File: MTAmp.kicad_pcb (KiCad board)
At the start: 2 copper layers, 67.3 x 86.4 mm, 31 parts, among them J1 IN3, J10 AMP1, J11 AMP2, J12 PROG, J2 PWR, J3 IN1, J4 IN4, J5 IN2, J6 OUT1, J7 OUT2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

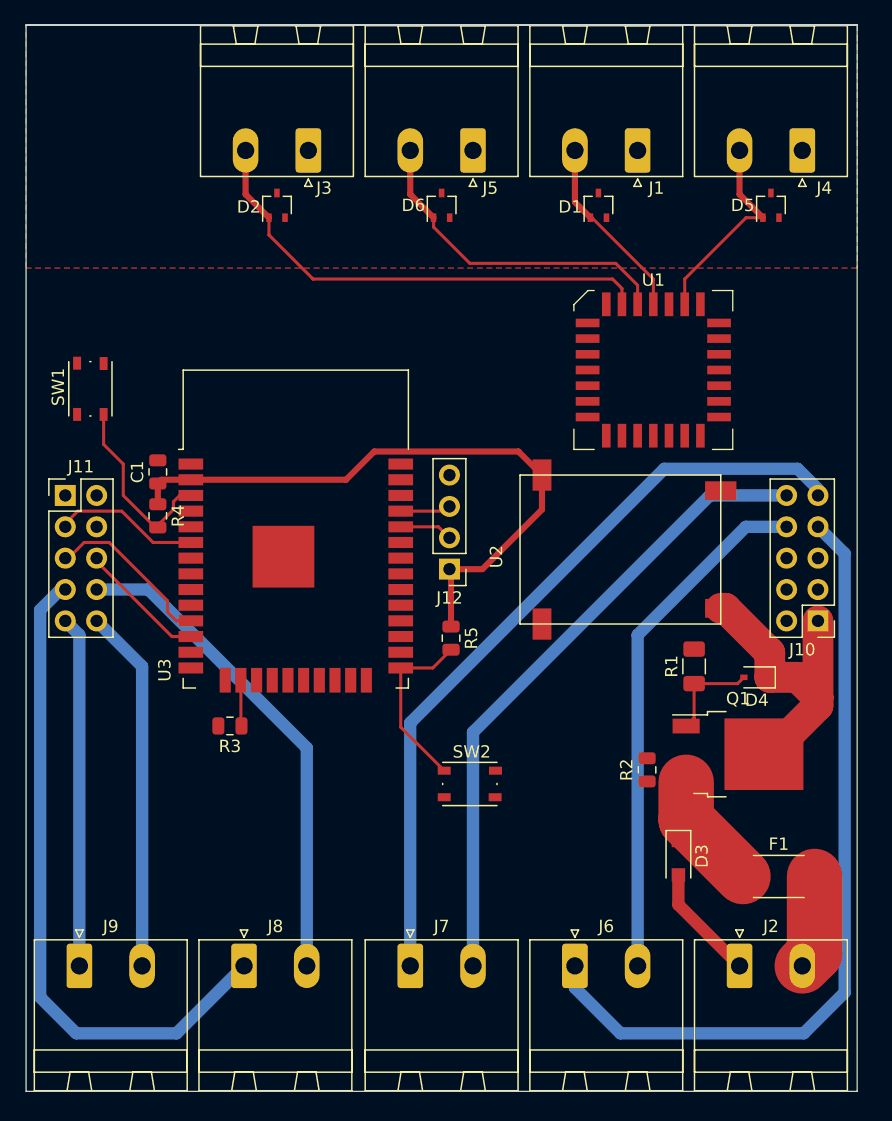
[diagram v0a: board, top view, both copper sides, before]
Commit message: Main PCB traced
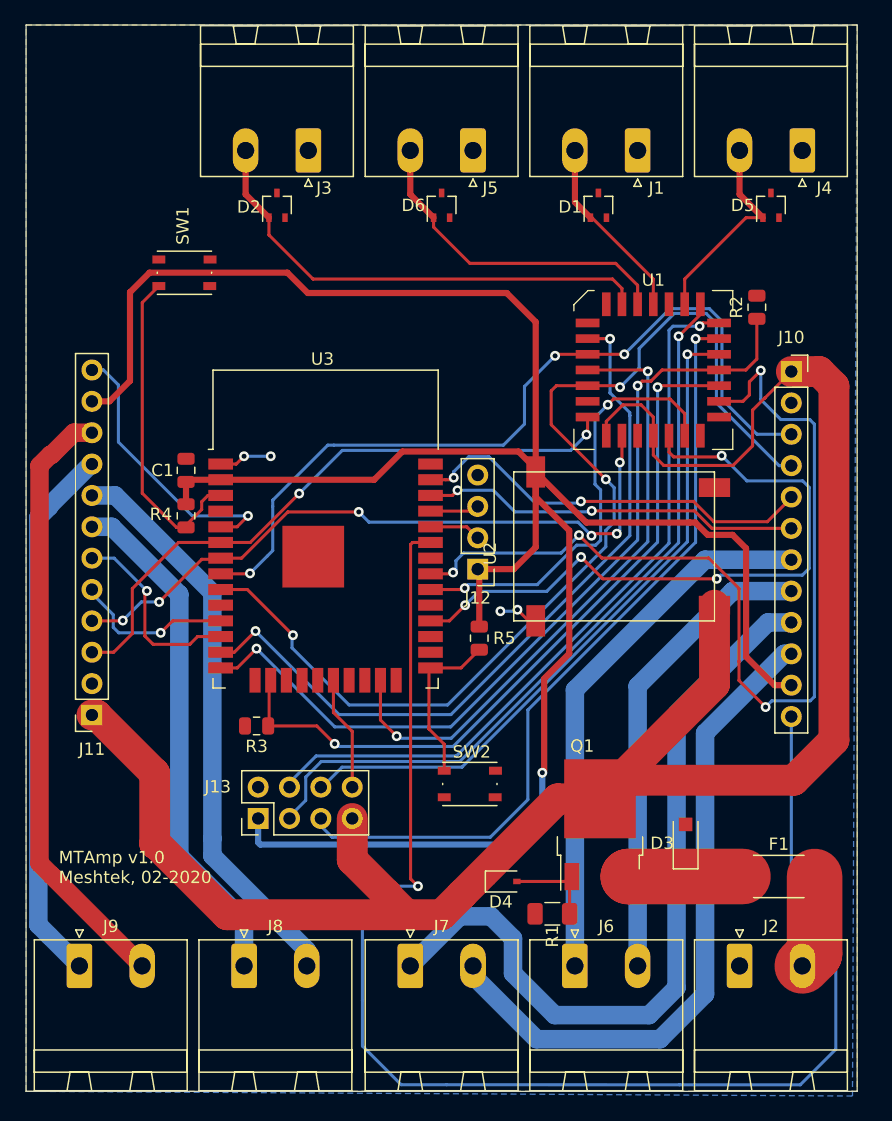
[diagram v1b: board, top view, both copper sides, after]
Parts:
- added J13: BT, Connector_PinHeader_2.54mm:PinHeader_2x04_P2.54mm_Vertical, F.Cu at (131.8, 90.9)
- J10, J11: footprint Connector_PinHeader_2.54mm:PinHeader_2x05_P2.54mm_Vertical -> Connector_PinSocket_2.54mm:PinSocket_1x12_P2.54mm_Vertical
- moved R2 38.5 mm to (172.2, 49.5)
- moved D4 26.3 mm to (151.7, 96.0), turned to 0 degrees
- moved R1 23.1 mm to (155.7, 98.7), turned to 180 degrees
- moved J10 20.3 mm to (175.0, 54.7), turned to 0 degrees
- moved J11 17.9 mm to (118.4, 82.5), turned to 180 degrees
- moved Q1 12.6 mm to (159.5, 91.4), turned to 90 degrees
- moved SW1 12.1 mm to (125.9, 46.7), turned to 0 degrees
- moved U3 2.41 mm to (137.3, 70.5)
- moved C1 2.29 mm to (126.0, 62.7)
- moved J12 2.29 mm to (149.6, 70.7)
- moved R4 2.29 mm to (126.0, 66.4)
- moved R5 2.29 mm to (149.7, 76.3)
- moved R3 2.16 mm to (131.7, 83.4)
- moved D3 1.42 mm to (166.4, 92.8), turned to 90 degrees
- moved U2 0.57 mm to (152.5, 74.9)
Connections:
- C1 pad 2: GNDD -> GNDA
- D3 pad 2: Net-(D3-Pad2) -> GNDA
- J10 pad 2: AGND -> GNDA
- J11 pad 2: AGND -> GNDA
- J12 pad 4: GNDD -> GNDA
- J2 pad 1: Net-(D3-Pad2) -> GNDA
- R1 pad 2: Net-(D3-Pad2) -> GNDA
- R2 pad 1: MT_Resest -> MT_Reset
- R2 pad 2: GNDD -> GNDA
- R3 pad 2: GNDD -> GNDA
- SW1 pad 1: GNDD -> GNDA
- SW2 pad 2: GNDD -> GNDA
- U1 pad 22: MT_Resest -> MT_Reset
- U2 pad 2: Net-(D3-Pad2) -> GNDA
- U3 pad 1: GNDD -> GNDA
- U3 pad 10: SD2 -> Net-(U3-Pad10)
- U3 pad 15: GNDD -> GNDA
- U3 pad 20: Net-(U3-Pad20) -> CONNECTED_BT
- U3 pad 33: Net-(U3-Pad33) -> CONNECTED1
- U3 pad 36: Net-(U3-Pad36) -> SD2
- U3 pad 38: GNDD -> GNDA
- U3 pad 39: GNDD -> GNDA
- U3 pad 5: Net-(U3-Pad5) -> CONNECTED2
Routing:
- net +3V3: track 51.6 -> 196.3 mm, vias 0 -> 1
- net +12V: track 24.9 -> 163.1 mm
- net CONNECTED1: track 0.00 -> 114.9 mm, vias 0 -> 1
- net MT_Out2: track 0.00 -> 88.1 mm, vias 0 -> 3
- net MT_AY2: track 0.00 -> 77.9 mm, vias 0 -> 4
- net MT_Reset: track 0.00 -> 69.6 mm, vias 0 -> 2
- net MT_Out1: track 0.00 -> 67.2 mm, vias 0 -> 3
- net MT_In7: track 0.00 -> 63.9 mm, vias 0 -> 1
- net MT_In5: track 0.00 -> 62.0 mm, vias 0 -> 1
- net MT_Data: track 0.00 -> 61.1 mm, vias 0 -> 2
- net MT_In6: track 0.00 -> 60.7 mm, vias 0 -> 1
- net MT_STB: track 3.72 -> 60.3 mm, vias 0 -> 2
- net MT_In8: track 0.00 -> 55.7 mm, vias 0 -> 1
- net MT_Out4: track 0.00 -> 55.1 mm, vias 0 -> 6
- net MT_AY0: track 0.00 -> 54.4 mm, vias 0 -> 4
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- added copper zone on B.Cu, net GNDA
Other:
- net class 3v3: clearance 0.2 -> 0.1
- net class Default: clearance 0.2 -> 0.1
- net class HighPwr: trace_width 1 -> 1.5
- net class IN12: clearance 0.2 -> 0.1
- net class InAudio: clearance 0.2 -> 0.1
- rule trace_clearance: 0.2 -> 0.1
- board text added: "MTAmp v1.0 Meshtek, 02-2020"

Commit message: Added some text on PCB
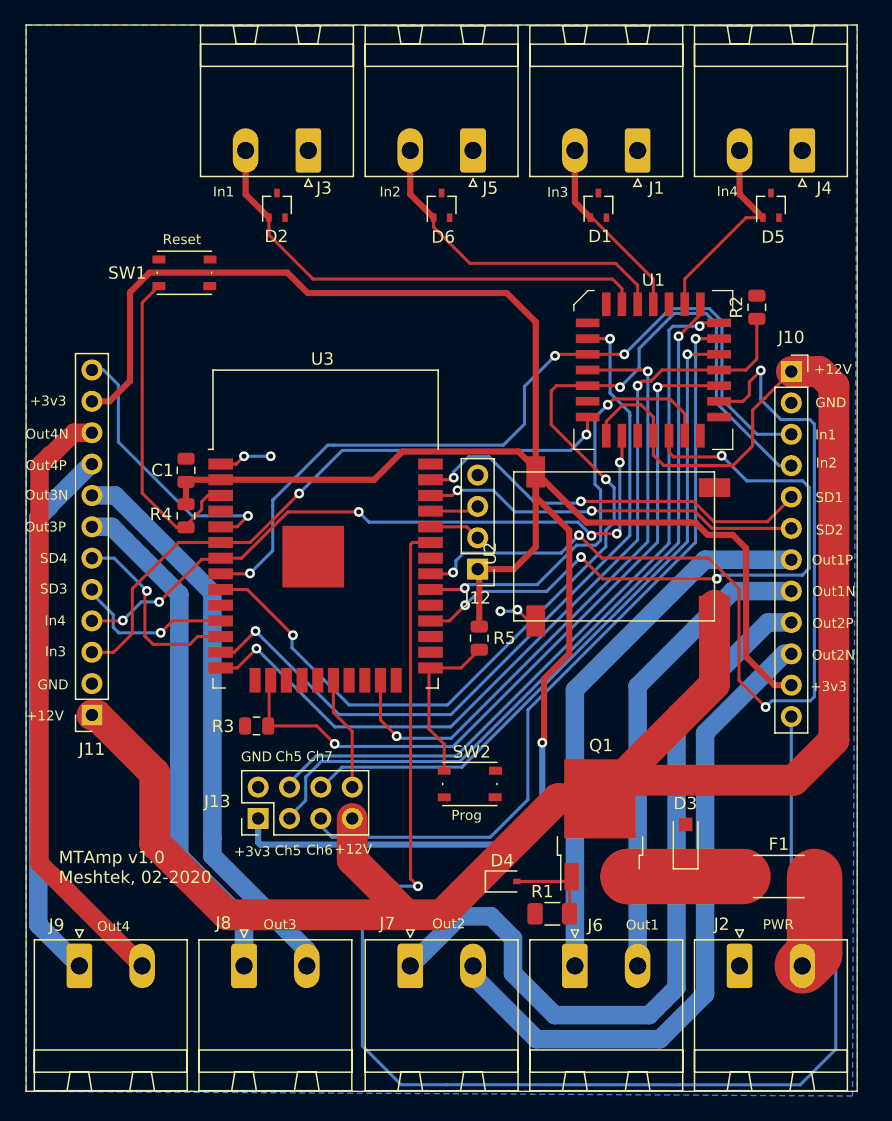
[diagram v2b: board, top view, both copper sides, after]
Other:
- board text added: "+12V"
- board text added: "+3v3"
- board text added: "Ch5"
- board text added: "Ch6"
- board text added: "Ch7"
- board text added: "GND"
- board text added: "In1"
- board text added: "In2"
- board text added: "In3"
- board text added: "In4"
- board text added: "Out1"
- board text added: "Out1N"
- board text added: "Out1P"
- board text added: "Out2"
- board text added: "Out2N"
- board text added: "Out2P"
- board text added: "Out3"
- board text added: "Out3N"
- board text added: "Out3P"
- board text added: "Out4"
- board text added: "Out4N"
- board text added: "Out4P"
- board text added: "PWR"
- board text added: "Prog"
- board text added: "Reset"
- board text added: "SD1"
- board text added: "SD2"
- board text added: "SD3"
- board text added: "SD4"
